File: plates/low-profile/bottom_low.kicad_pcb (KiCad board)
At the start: 2 copper layers, 260.1 x 100.6 mm, 12 parts, among them X1 5.5mm, X10 5.5mm, X2 5.5mm, X3 5.5mm, X4 5.5mm, X5 5.5mm, X6 5.5mm, X7 5.5mm, X8 5.5mm, X9 5.5mm

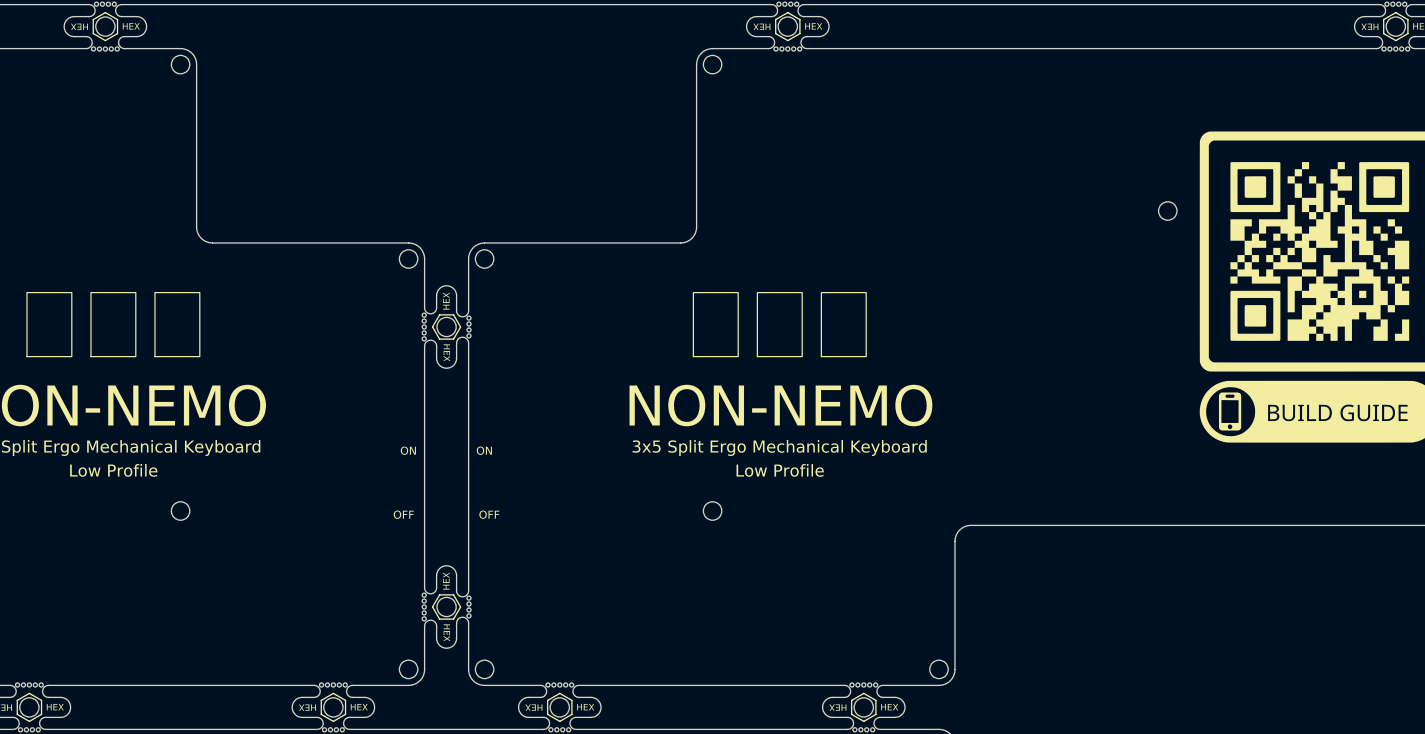
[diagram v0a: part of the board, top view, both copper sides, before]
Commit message: reset switch (#6)
* added reset switch

* Low Profile

pogopin and reset button

* MX Profile

pogopin and reset switch

* MX Profile PCB

* Chimera

pogopin and reset switch

* version

* updated README.md
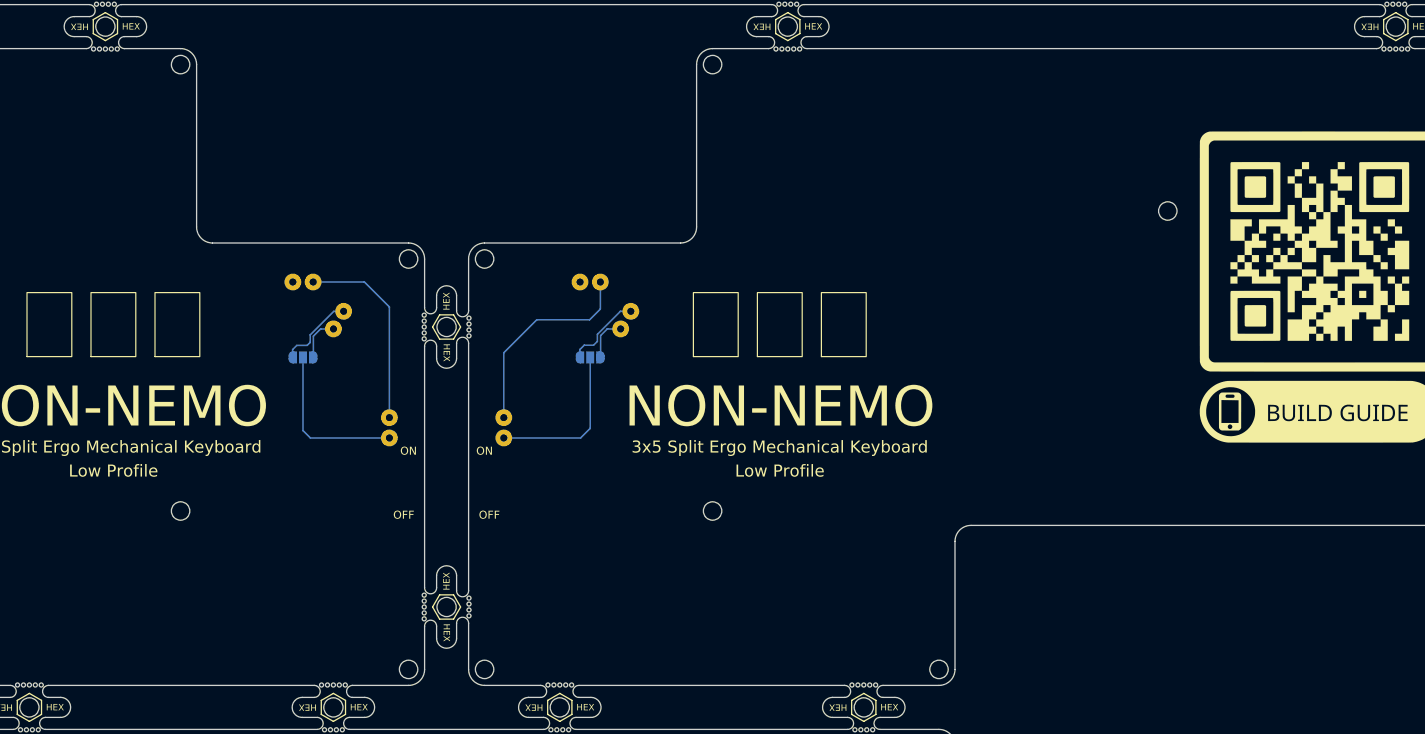
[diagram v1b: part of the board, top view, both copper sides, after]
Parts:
- added J1: Conn_01x02, TB2086_MISC:Pogopin_1x02_P2.54mm, F.Cu at (135.1, 85.1)
- added J2: Conn_01x02, TB2086_MISC:Pogopin_1x02_P2.54mm, F.Cu at (171.0, 85.1)
- added J3: Conn_01x02, TB2086_MISC:Pogopin_1x02_P2.54mm, F.Cu at (130.7, 80.4)
- added J4: Conn_01x02, TB2086_MISC:Pogopin_1x02_P2.54mm, F.Cu at (166.6, 80.4)
- added J5: Conn_01x02, TB2086_MISC:Pogopin_1x02_P2.54mm, F.Cu at (141.5, 98.6)
- added J6: Conn_01x02, TB2086_MISC:Pogopin_1x02_P2.54mm, F.Cu at (155.8, 98.6)
- added JP1: SolderJumper_3_Open, TB2086_MISC:SolderJumper-3_P1.3mm_Open_RoundedPad1.0x1.5mm, F.Cu at (130.7, 89.8)
- added JP2: SolderJumper_3_Open, TB2086_MISC:SolderJumper-3_P1.3mm_Open_RoundedPad1.0x1.5mm, F.Cu at (166.6, 89.8)
- moved X7 161.3 mm to (267.3, 45.7)
- moved X5 160.8 mm to (30.0, 45.7), turned to 90 degrees
- moved X9 85.2 mm to (151.4, 121.0), turned to 0 degrees
- moved X6 76.0 mm to (106.0, 45.7)
- moved X8 76.0 mm to (191.3, 45.7)
- moved X3 66.3 mm to (200.8, 136.3)
- moved X1 57.0 mm to (96.5, 136.3), turned to -90 degrees
- moved X2 38.0 mm to (134.5, 136.3)
- moved X4 38.0 mm to (162.8, 136.3)
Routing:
- net RST_r: track 0.00 -> 25.8 mm
- net RST: track 0.00 -> 24.7 mm
- net BAT: track 0.00 -> 20.3 mm
- net BAT_r: track 0.00 -> 20.2 mm
- net BAT_c: track 0.00 -> 9.89 mm
- net BAT_cr: track 0.00 -> 9.86 mm
- net BAT_xr: track 0.00 -> 5.58 mm
- net BAT_x: track 0.00 -> 5.54 mm
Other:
- board text added: "B+"
- board text added: "GND"
- board text added: "MINI"
- board text added: "RST"
- board text added: "XIAO"

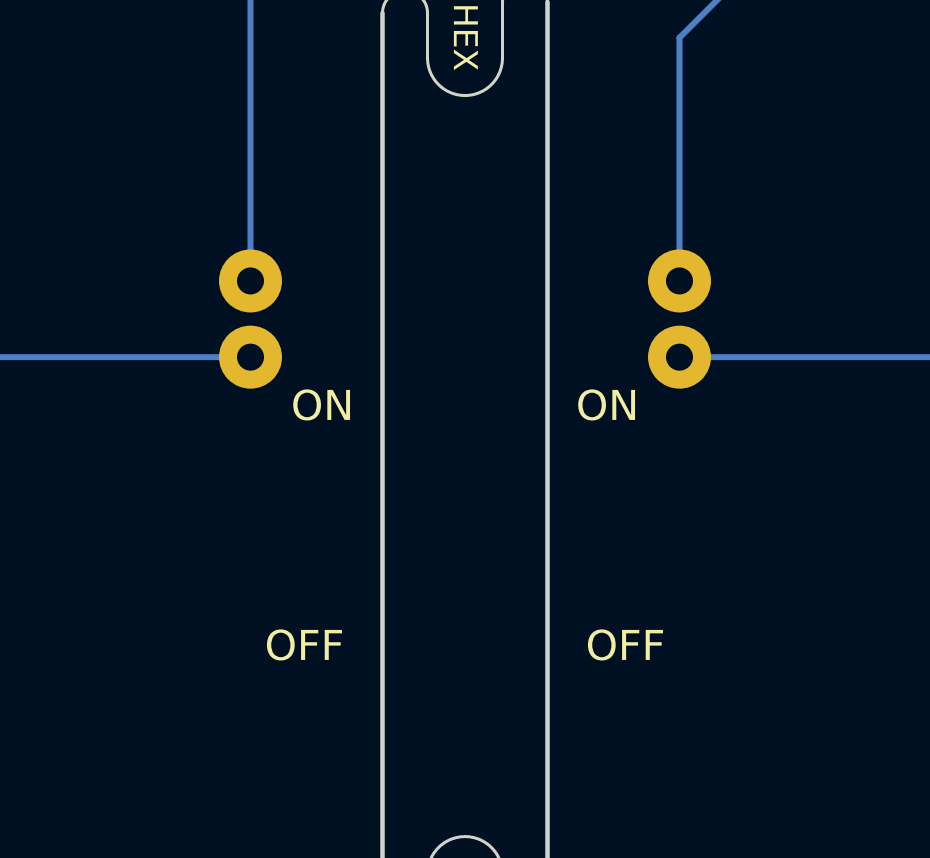
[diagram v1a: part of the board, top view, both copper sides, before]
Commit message: added shells for low profile
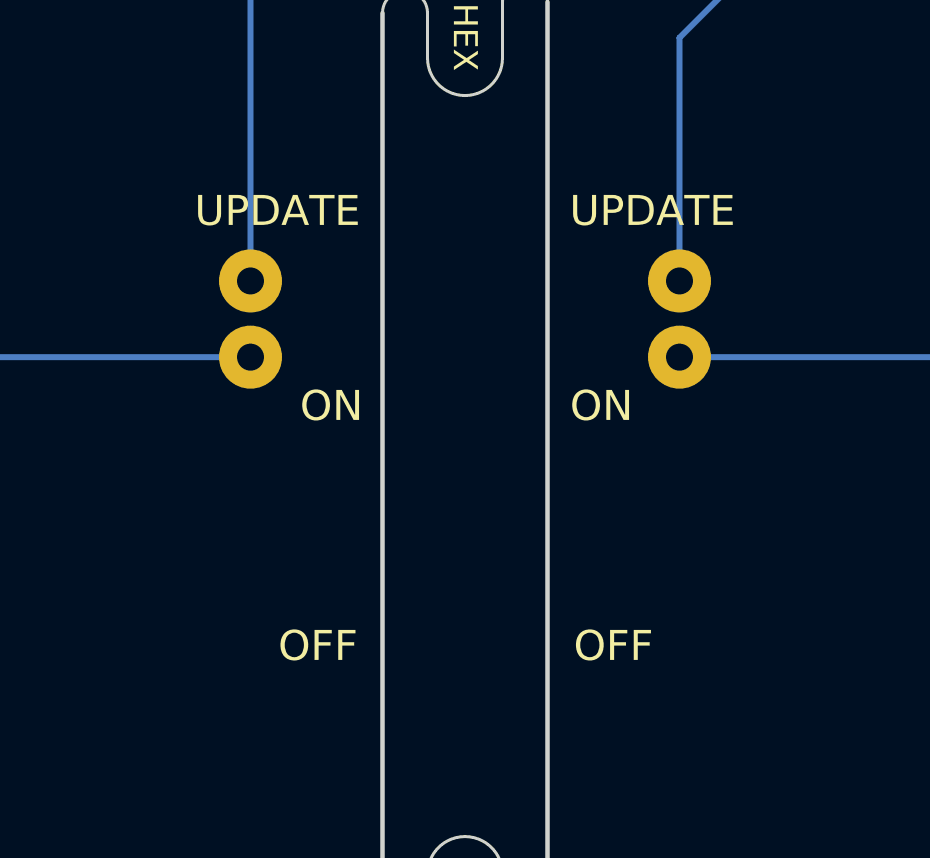
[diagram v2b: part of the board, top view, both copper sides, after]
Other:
- board text added: "UPDATE"
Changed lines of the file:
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@@
-		)
-	)
-	(gr_text "OFF"
-		(at 143.3 109.5 0)
-		(layer "B.SilkS" knockout)
-		(effects
-			(font
-				(size 1 1)
-				(thickness 0.15)
-			)
-			(justify mirror)
 		)
 	)
@@
 		)
 	)
-	(gr_text "ON"
-		(at 153.4 101.5 0)
-		(layer "B.SilkS" knockout)
-		(effects
-			(font
-				(size 1 1)
-				(thickness 0.15)
-			)
-			(justify mirror)
-		)
-	)
 	(gr_text "GND"
 		(at 165.3 82.3775 0)
@@
 		)
 	)
-	(gr_text "ON"
-		(at 143.9 101.5 0)
-		(layer "B.SilkS" knockout)
-		(effects
-			(font
-				(size 1 1)
-				(thickness 0.15)
-			)
-			(justify mirror)
-		)
-	)
 	(gr_text "Low Profile"
 		(at 115.5 129.5 0)
@@
 				(face "KiCad Font")
 				(size 1.5 1.5)
-				(thickness 0.15)
-			)
-			(justify mirror)
-		)
-	)
-	(gr_text "OFF"
-		(at 154 109.5 0)
-		(layer "B.SilkS" knockout)
-		(effects
-			(font
-				(size 1 1)
 				(thickness 0.15)
 			)
@@
 	)
 	(gr_text "OFF"
-		(at 154 109.5 0)
+		(at 153.6 109.5 0)
 		(layer "F.SilkS" knockout)
 		(effects
@@
 	)
 	(gr_text "ON"
-		(at 153.4 101.5 0)
+		(at 153.2 101.5 0)
 		(layer "F.SilkS" knockout)
 		(effects
@@
 	)
 	(gr_text "ON"
-		(at 143.9 101.5 0)
+		(at 144.2 101.5 0)
 		(layer "F.SilkS" knockout)
 		(effects
@@
 		)
 	)
+	(gr_text "UPDATE"
+		(at 154.9 95 0)
+		(layer "F.SilkS" knockout)
+		(effects
+			(font
+				(size 1 1)
+				(thickness 0.15)
+			)
+		)
+	)
+	(gr_text "UPDATE"
+		(at 142.4 95 0)
+		(layer "F.SilkS" knockout)
+		(effects
+			(font
+				(size 1 1)
+				(thickness 0.15)
+			)
+		)
+	)
 	(gr_text "OFF"
-		(at 143.3 109.5 0)
+		(at 143.75 109.5 0)
 		(layer "F.SilkS" knockout)
 		(effects
